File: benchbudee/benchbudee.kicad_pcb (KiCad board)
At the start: 2 copper layers, 2 parts

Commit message: Setting up for layout
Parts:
- moved Arduino MEGA 392.1 mm to (-186.9, 90.4)
- moved Arduino UNO 392.1 mm to (-186.9, 33.3)
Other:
- board outline added: 165.1 x 63.5 mm
- copper layers 2 -> 4
- rule trace_min: 0.254 -> 0.1524
- rule via_min_drill: 0.508 -> 0.3302
- rule via_min_size: 0.889 -> 0.508
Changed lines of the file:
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@@
-(kicad_pcb (version 3) (host pcbnew "(2013-07-07 BZR 4022)-stable")
+(kicad_pcb (version 3) (host pcbnew "(2014-03-08 BZR 4739)-product")
   (general
     (links 0)
     (no_connects 0)
-    (area 157.150999 89.341 265.759001 204.029)
+    (area 157.150999 88.991 265.759001 204.229)
     (thickness 1.6)
-    (drawings 0)
+    (drawings 4)
     (tracks 0)
     (zones 0)
@@
   (layers
     (15 F.Cu signal)
+    (2 PWR power)
+    (1 GND power)
     (0 B.Cu signal)
     (16 B.Adhes user)
@@
     (22 B.Mask user)
     (23 F.Mask user)
-    (24 Dwgs.User user)
-    (25 Cmts.User user)
-    (26 Eco1.User user)
-    (27 Eco2.User user)
     (28 Edge.Cuts user)
   )
   (setup
     (last_trace_width 0.254)
+    (user_trace_width 0.1524)
     (trace_clearance 0.254)
     (zone_clearance 0.508)
     (zone_45_only no)
-    (trace_min 0.254)
+    (trace_min 0.1524)
     (segment_width 0.2)
     (edge_width 0.1)
     (via_size 0.889)
     (via_drill 0.635)
-    (via_min_size 0.889)
-    (via_min_drill 0.508)
+    (via_min_size 0.508)
+    (via_min_drill 0.3302)
+    (user_via 0.508 0.3302)
     (uvia_size 0.508)
     (uvia_drill 0.127)
     (uvias_allowed no)
-    (uvia_min_size 0.508)
+    (uvia_min_size 0.381)
     (uvia_min_drill 0.127)
     (pcb_text_width 0.3)
@@
   )
   (module Arduino_UNO (layer F.Cu)
-    (at 195.58 119.38)
+    (at -186.944 33.274)
     (fp_text reference "Arduino UNO" (at 0 -29.21) (layer F.SilkS) hide
       (effects (font (size 1 1) (thickness 0.15)))
@@
   )
   (module Arduino_MEGA (layer F.Cu)
-    (at 195.58 176.53)
+    (at -186.944 90.424)
     (fp_text reference "Arduino MEGA" (at 0 -29.21) (layer F.SilkS) hide
       (effects (font (size 1 1) (thickness 0.15)))
@@
     (fp_line (start -31.75 -25.4) (end -31.75 25.4) (layer Eco1.User) (width 0.15))
   )
+  (gr_line (start 110.236 111.76) (end 110.236 175.26) (angle 90) (layer Edge.Cuts) (width 0.1))
+  (gr_line (start 275.336 111.76) (end 110.236 111.76) (angle 90) (layer Edge.Cuts) (width 0.1))
+  (gr_line (start 275.336 175.26) (end 275.336 111.76) (angle 90) (layer Edge.Cuts) (width 0.1))
+  (gr_line (start 110.236 175.26) (end 275.336 175.26) (angle 90) (layer Edge.Cuts) (width 0.1))
 )

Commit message: Relay module footprints done
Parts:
- removed Arduino MEGA: Val**, Arduino_MEGA
- removed Arduino UNO: Val**, Arduino_UNO
- added D1: LG 0971-KN-1, LEDs:LED-0603, F.Cu at (240.1, 178.5)
- added D2: B130-13-F, BenchBudEE:SMA, F.Cu at (247.1, 166.0)
- added K1: 1461069-5, BenchBudEE:TE-SPDT, F.Cu at (220.0, 171.5)
- added Q1: 2N3904, SMD_Packages:SOT23EBC, F.Cu at (247.4, 173.7)
- added R1: 500, SMD_Packages:SM0805, F.Cu at (245.5, 177.8)
- added R2: 200, SMD_Packages:SM0805, F.Cu at (252.1, 171.3)
- added R3: 0, SMD_Packages:SM0805, F.Cu at (245.5, 180.1)
- added R4: 100, SMD_Packages:SM0805, F.Cu at (249.4, 176.5)
- added R5: 0, SMD_Packages:SM0805, F.Cu at (252.1, 173.6)
- added R6: 0, SMD_Packages:SM0805, F.Cu at (249.4, 178.8)
- added U1: LTV-816S, BenchBudEE:4-SMD, F.Cu at (239.3, 173.6)
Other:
- rule pad_to_mask_clearance: 0 -> 0.254

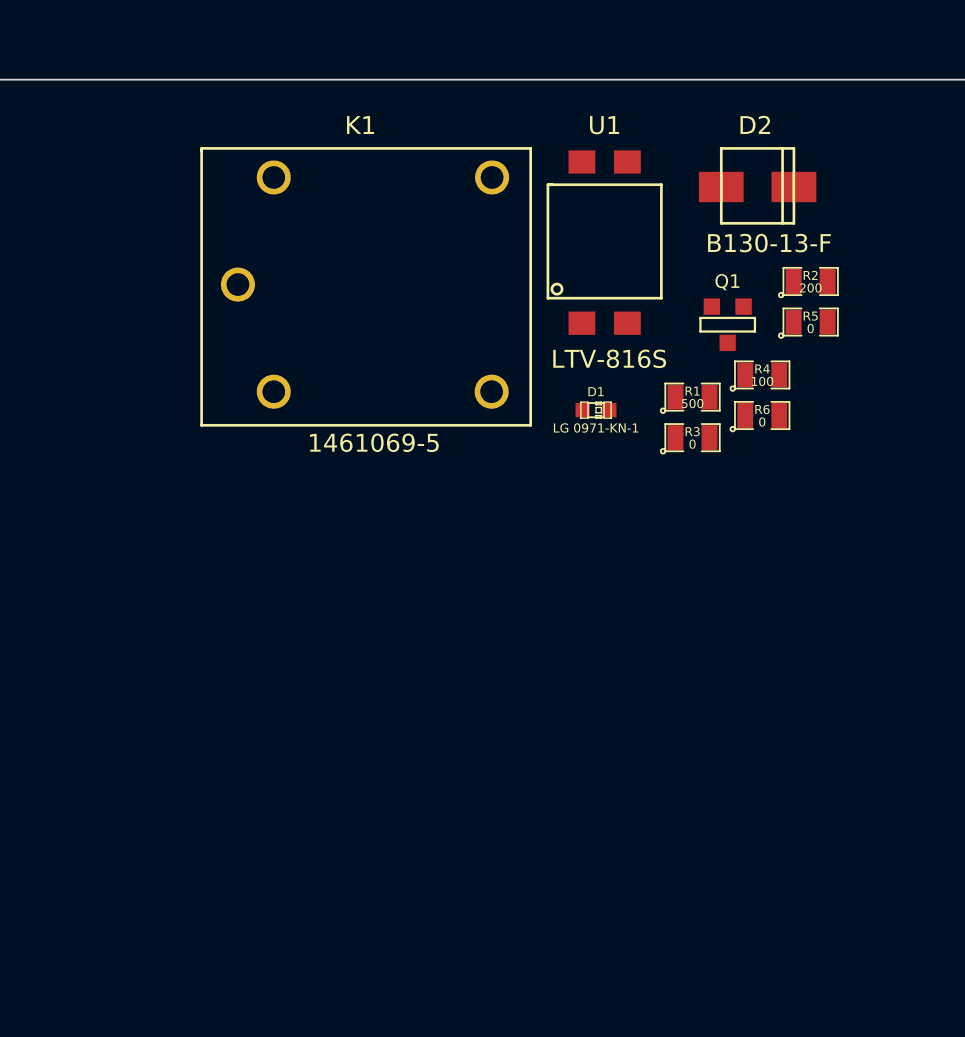
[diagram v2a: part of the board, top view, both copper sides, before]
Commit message: Schematic and associations for the thermocouple module
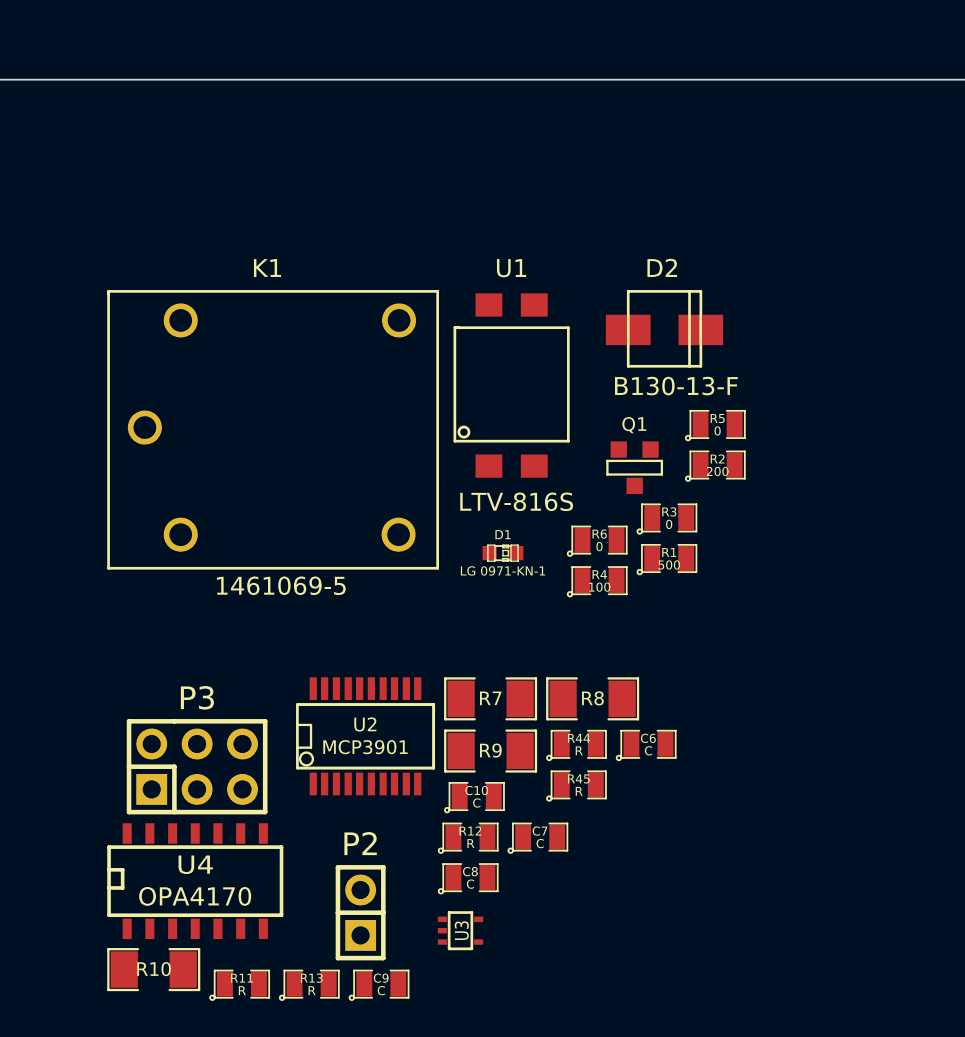
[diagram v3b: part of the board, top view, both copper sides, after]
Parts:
- added C10: C, SMD_Packages:SM0805, F.Cu at (233.4, 200.1)
- added C6: C, SMD_Packages:SM0805, F.Cu at (243.0, 197.2)
- added C7: C, SMD_Packages:SM0805, F.Cu at (237.0, 202.4)
- added C8: C, SMD_Packages:SM0805, F.Cu at (233.1, 204.7)
- added C9: C, SMD_Packages:SM0805, F.Cu at (228.1, 210.6)
- added P2: CONN_2, Pin_Headers:Pin_Header_Straight_2x01, F.Cu at (226.9, 206.6)
- added P3: CONN_3X2, Pin_Headers:Pin_Header_Straight_2x03, F.Cu at (217.8, 198.5)
- added R10: R, SMD_Packages:SM1206, F.Cu at (215.3, 209.8)
- added R11: R, SMD_Packages:SM0805, F.Cu at (220.3, 210.6)
- added R12: R, SMD_Packages:SM0805, F.Cu at (233.1, 202.4)
- added R13: R, SMD_Packages:SM0805, F.Cu at (224.2, 210.6)
- added R44: R, SMD_Packages:SM0805, F.Cu at (239.1, 197.2)
- added R45: R, SMD_Packages:SM0805, F.Cu at (239.1, 199.5)
- added R7: R, SMD_Packages:SM1206, F.Cu at (234.2, 194.7)
- added R8: R, SMD_Packages:SM1206, F.Cu at (239.9, 194.7)
- added R9: R, SMD_Packages:SM1206, F.Cu at (234.2, 197.6)
- added U2: MCP3901, SMD_Packages:SSOP20, F.Cu at (227.2, 196.8)
- added U3: LMT84, SMD_Packages:SOT353, F.Cu at (232.5, 207.6)
- added U4: OPA4170, SMD_Packages:SO14E, F.Cu at (217.7, 204.7)
- moved R4 14.7 mm to (240.3, 188.1)
- moved R2 11.5 mm to (246.9, 181.6)
- moved R6 11.5 mm to (240.3, 185.8)
- moved K1 9.55 mm to (214.8, 179.5)
- moved D1 9.55 mm to (234.9, 186.5)
- moved D2 9.55 mm to (241.9, 174.0)
- moved Q1 9.55 mm to (242.2, 181.7)
- moved U1 9.55 mm to (234.1, 181.6)
- moved R1 9.13 mm to (244.2, 186.8)
- moved R5 7.74 mm to (246.9, 179.3)
- moved R3 4.68 mm to (244.2, 184.5)

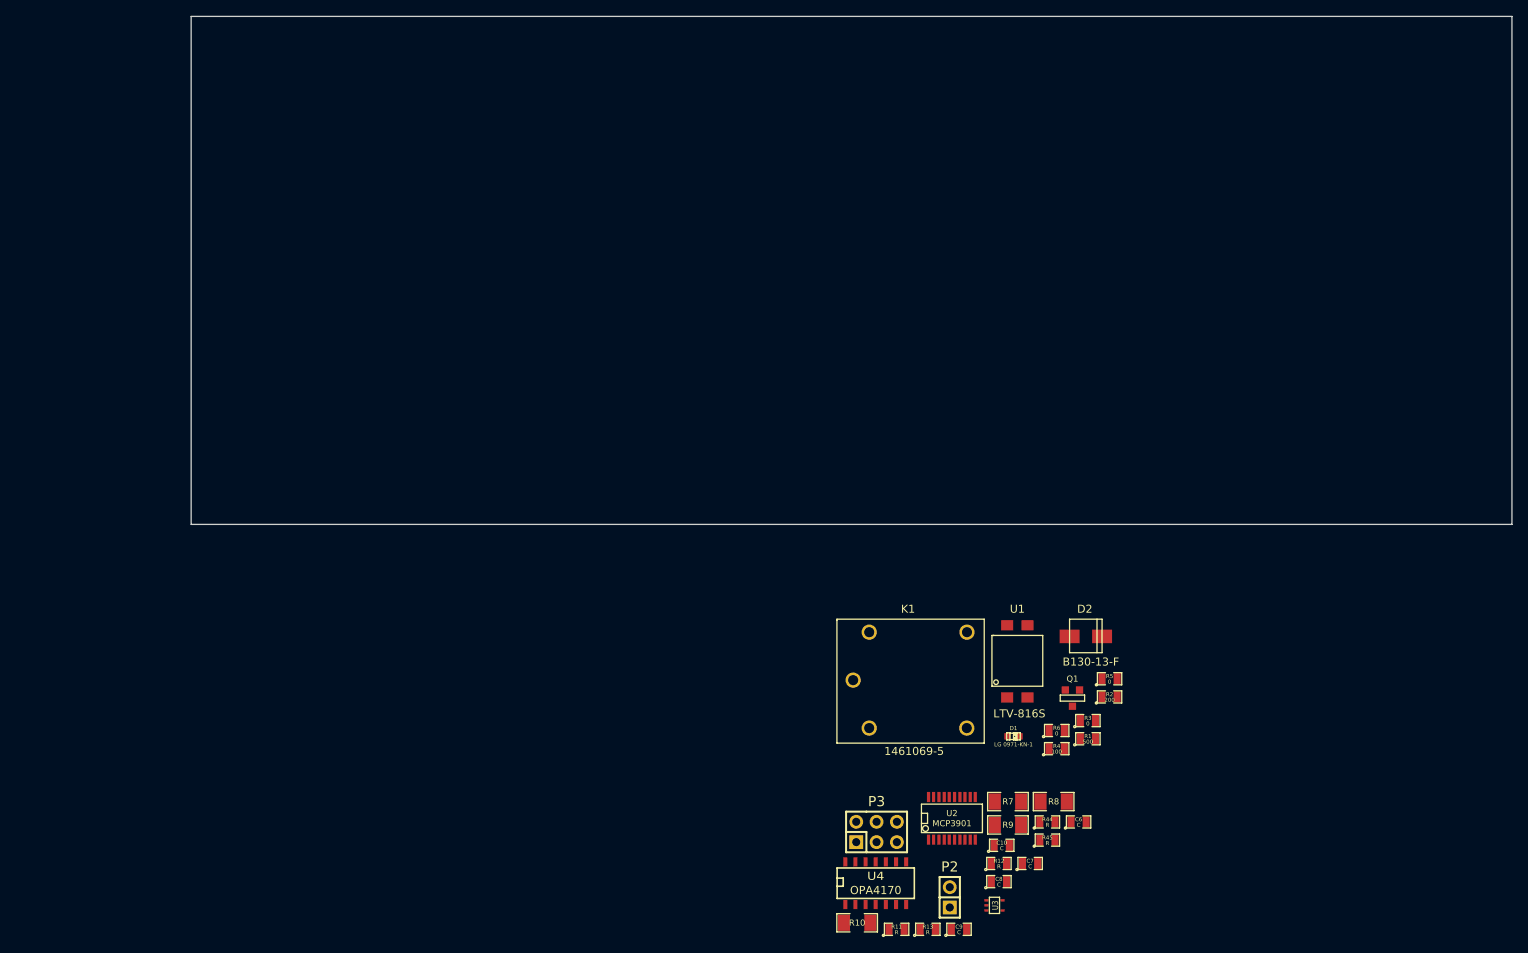
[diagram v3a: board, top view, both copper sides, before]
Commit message: Initial placement of thermocouple module
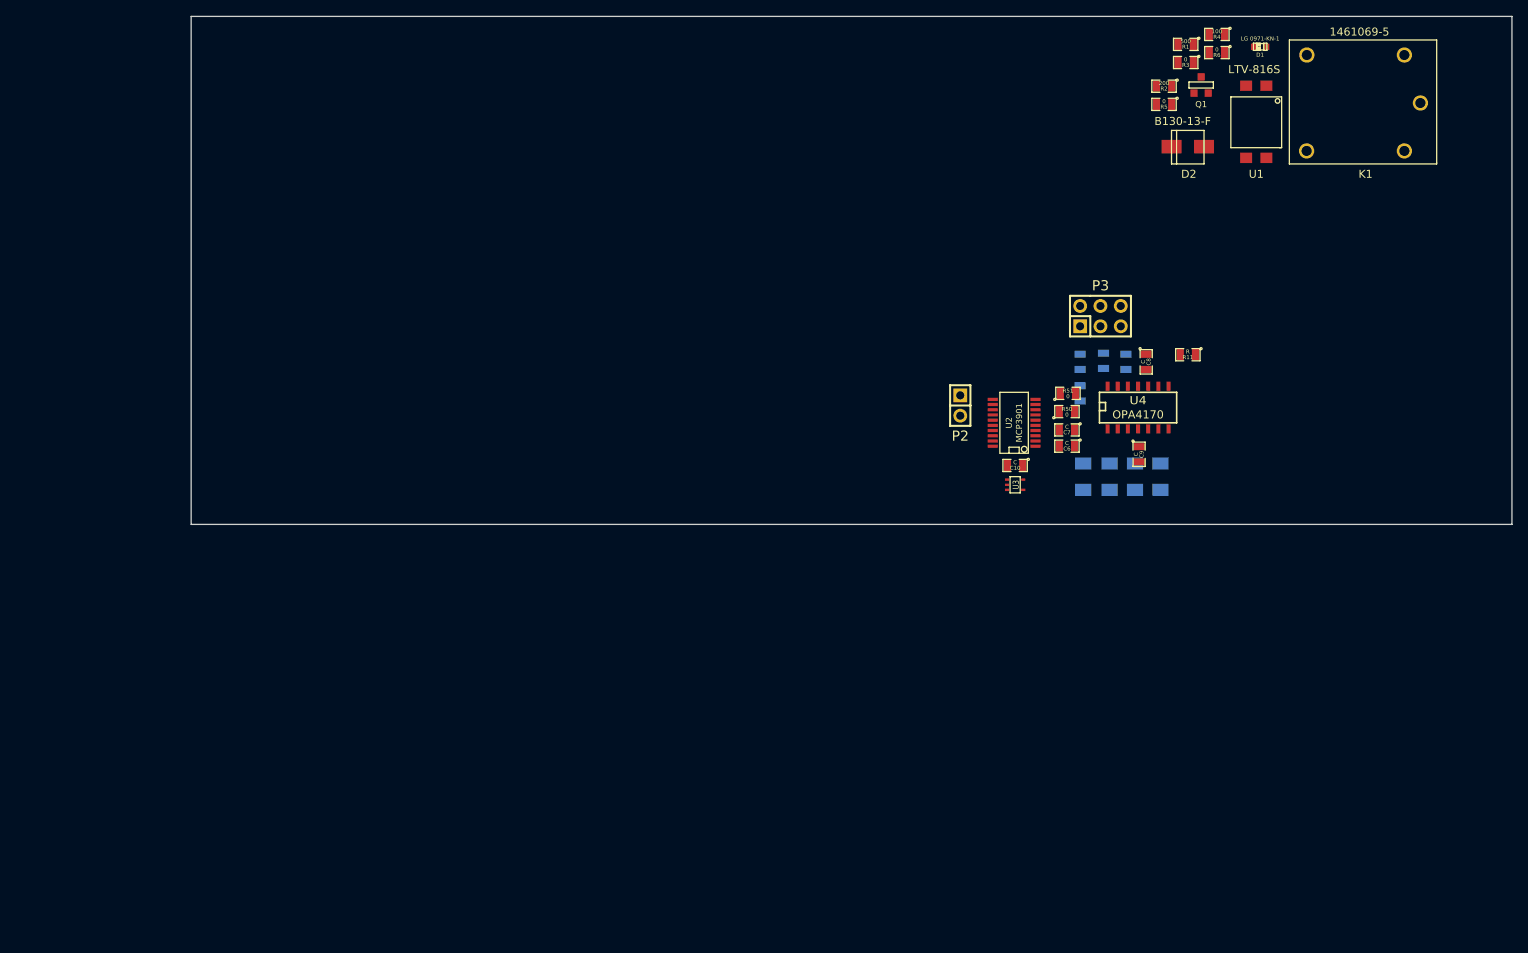
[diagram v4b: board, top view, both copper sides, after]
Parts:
- added R50: 0, SMD_Packages:SM0805, F.Cu at (241.6, 145.9)
- added R51: 0, SMD_Packages:SM0805, F.Cu at (241.7, 143.6)
- R10, R12, R13, R44, R45, R7, R8, R9: moved to B.Cu
- moved K1 101.2 mm to (285.7, 107.3), turned to 180 degrees
- moved D1 91.5 mm to (265.7, 100.3), turned to 180 degrees
- moved R4 91.5 mm to (260.3, 98.8), turned to 180 degrees
- moved R1 87.7 mm to (256.4, 100.0), turned to 180 degrees
- moved R6 87.1 mm to (260.3, 101.0), turned to 180 degrees
- moved R3 83.2 mm to (256.4, 102.3), turned to 180 degrees
- moved U1 83.0 mm to (266.5, 105.2), turned to 180 degrees
- moved R11 80.5 mm to (256.7, 138.8), turned to 180 degrees
- moved Q1 78.3 mm to (258.3, 105.1), turned to 180 degrees
- moved R2 76.6 mm to (253.7, 105.2), turned to 180 degrees
- moved R5 72.1 mm to (253.7, 107.5), turned to 180 degrees
- moved P3 70.3 mm to (245.7, 134.0)
- moved R13 69.7 mm to (243.2, 143.6), turned to 270 degrees
- moved U4 67.9 mm to (250.4, 145.3)
- moved C8 67.5 mm to (251.5, 139.7), turned to 270 degrees
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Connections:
- net Net-(R7-Pad1) renamed /Thermocouple/CH0+
- net Net-(U2-Pad7) renamed /Thermocouple/CH1+
- C10 pad 2: Net-(C10-Pad2) -> AGND
- C9 pad 2: AGND -> /Thermocouple/CH0-
- U2 pad 5: AGND -> /Thermocouple/CH0-
- U2 pad 6: Net-(C10-Pad2) -> /Thermocouple/CH1-
- U3 pad 1: Net-(C10-Pad2) -> AGND
- U3 pad 2: Net-(C10-Pad2) -> AGND
- U3 pad 5: Net-(C10-Pad2) -> AGND
